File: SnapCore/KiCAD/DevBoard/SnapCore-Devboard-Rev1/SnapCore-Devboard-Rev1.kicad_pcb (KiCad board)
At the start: 4 copper layers, 26.8 x 55.9 mm, 58 parts, among them J2 USB_C_Receptacle_USB2.0_16P, J3 Conn_01x18_Pin, Q1 AO3407A, SW2 TS-1187A, U1 nRF52840-QIXX, U2 XC6220B331MR, U5 TP4056-42-ESOP8, Y1 32.768KHz, Y2 32MHz

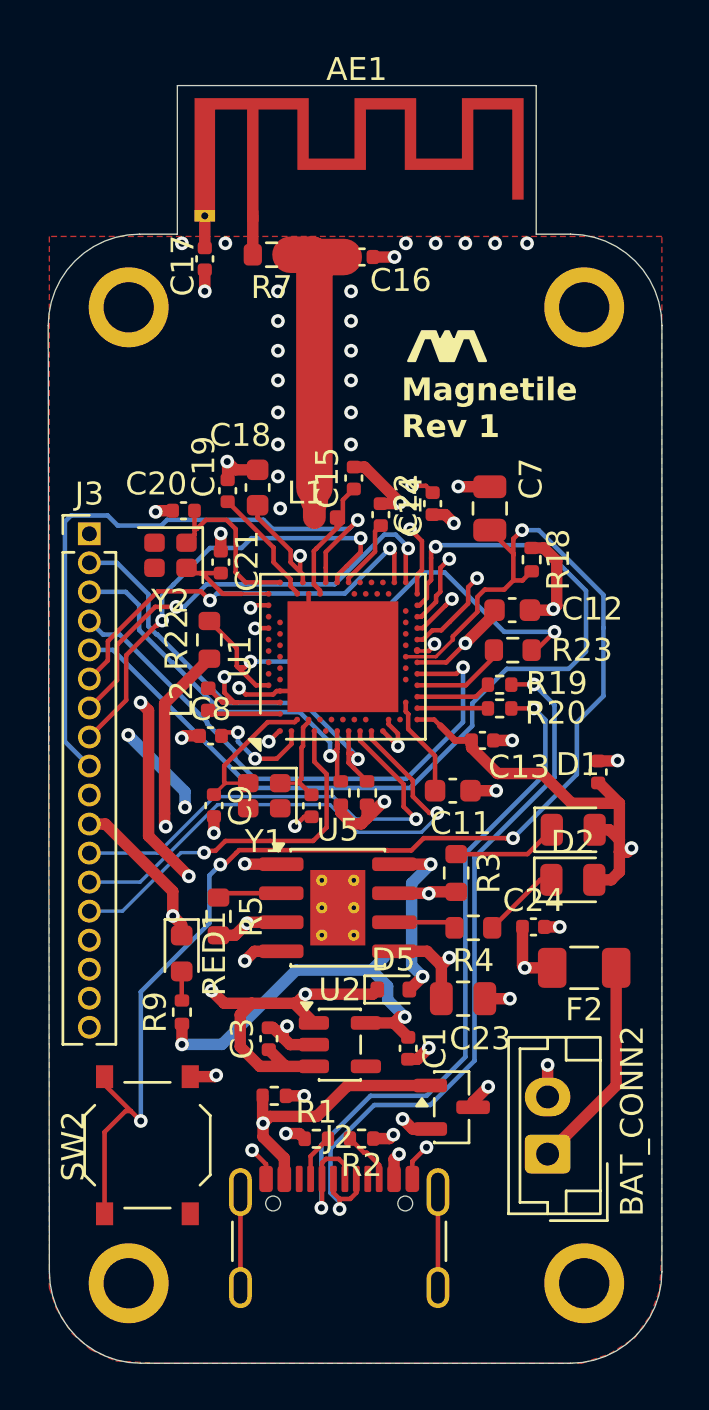
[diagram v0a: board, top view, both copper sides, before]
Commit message: Updated Devboard to use Chip Antenna instead of PCB Antenna for easier RF matching
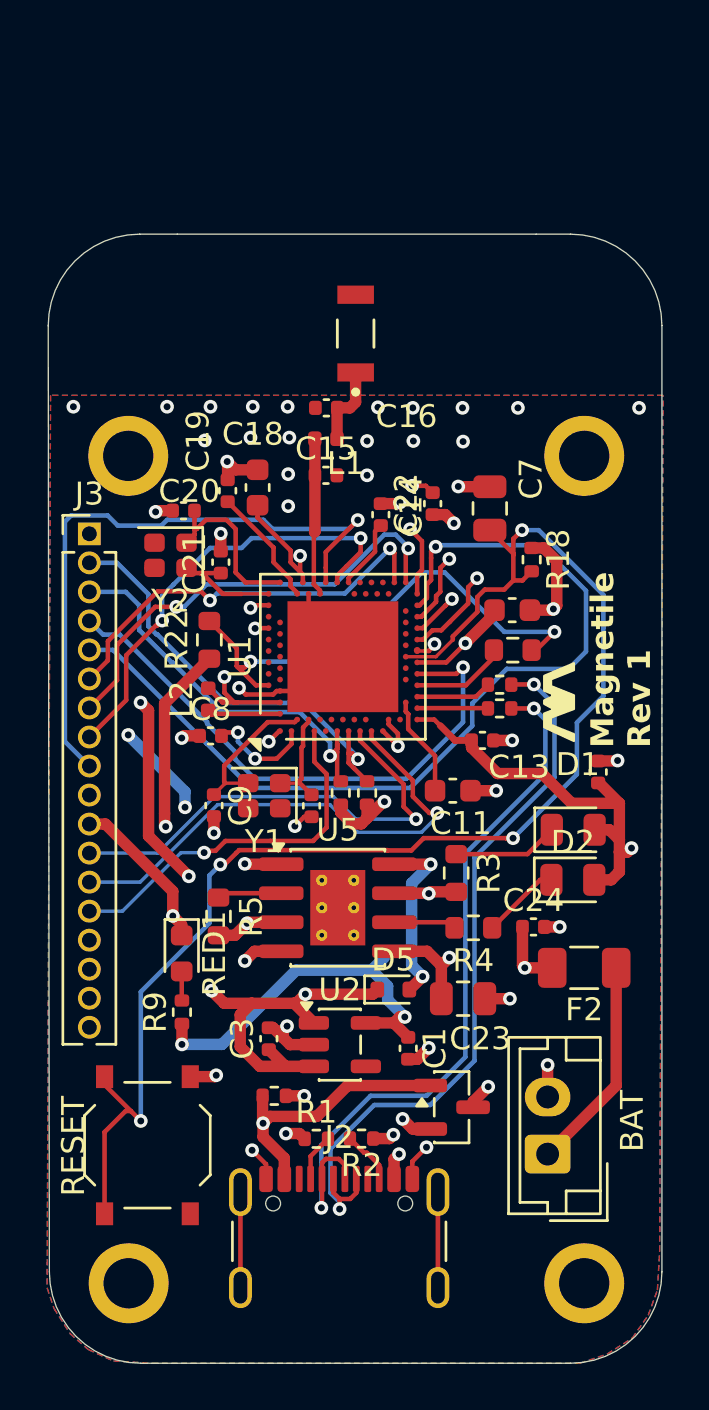
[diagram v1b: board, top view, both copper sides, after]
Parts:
- removed AE1: SWRA117D_2.4Ghz, RF_Antenna:Texas_SWRA117D_2.4GHz_Right
- removed C17: 1nF, Capacitor_SMD:C_0402_1005Metric
- removed R7: 0R, Resistor_SMD:R_0603_1608Metric
- added AE2: AMCA31-2R450G-S1F-T3, AMCA31-2R450G-S1F-T3:XDCR_AMCA31-2R450G-S1F-T3, F.Cu at (111.7, 86.5)
- moved H3 42.7 mm to (121.7, 128.0)
- moved H2 36.2 mm to (121.7, 91.8)
- moved C16 6.78 mm to (110.4, 89.7), turned to 180 degrees
- moved H4 6.50 mm to (101.8, 91.8)
- moved L1 3.45 mm to (110.4, 91.0), turned to 0 degrees
- moved C15 1.23 mm to (110.4, 92.7), turned to 0 degrees
- turned C21 to -90 degrees
- renumbered BAT_CONN2 to BAT, SW2 to RESET
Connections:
- C21 pad 1: XC2 -> GND
- C21 pad 2: GND -> XC2
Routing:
- net Net-(AE2-A): track 13.8 -> 3.56 mm
- net GND: track 67.6 -> 63.1 mm, vias 53 -> 49
- net Net-(AE1-FEED): track 1.70 -> 0.00 mm
- net Net-(AE1-PCB_Trace): track 1.40 -> 0.00 mm
- net ANT_H23: track 5.90 -> 6.92 mm
- added copper zone on B.Cu, net GND
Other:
- board size 26.8 x 55.9 mm -> 26.8 x 49.4 mm

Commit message: Removed unecessary silkscreen, Fixed small layout issue
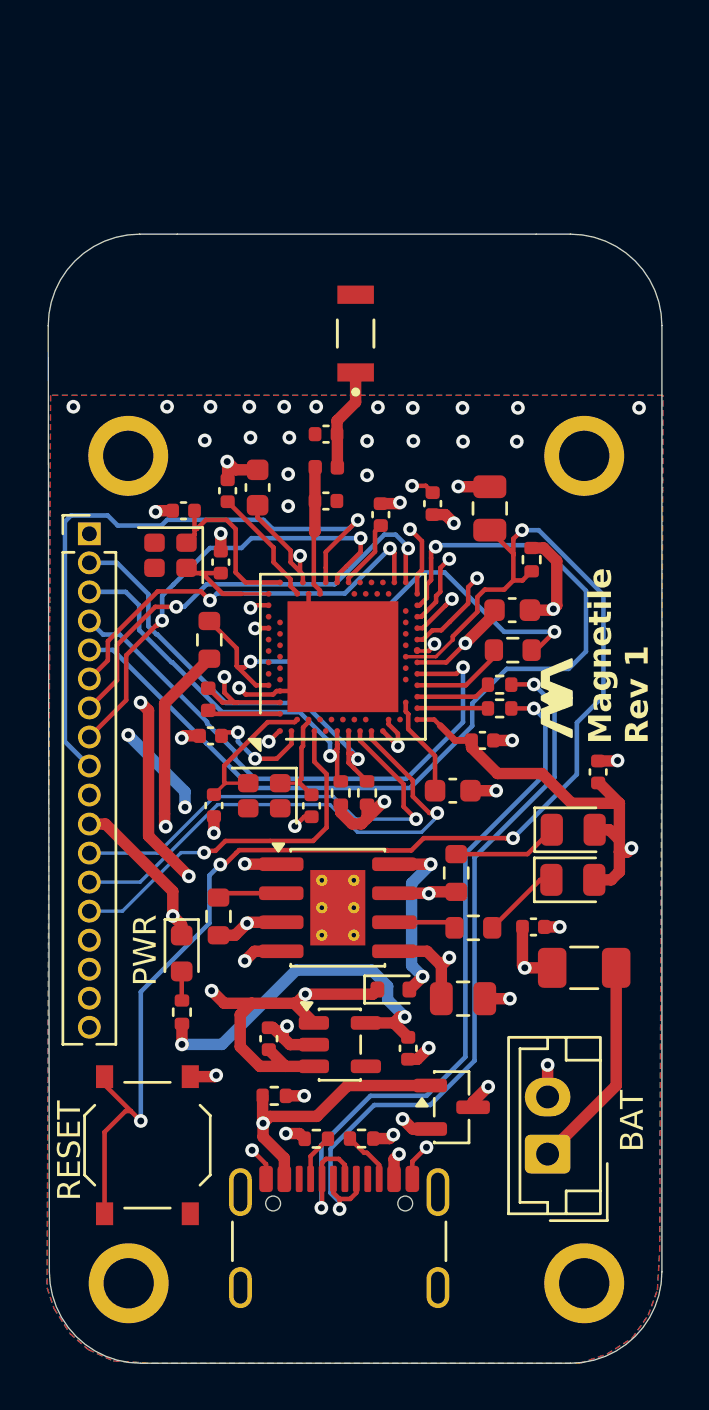
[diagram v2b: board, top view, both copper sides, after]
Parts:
- moved L1 1.25 mm to (110.4, 92.3)
- moved C16 1.15 mm to (110.4, 90.8)
- moved C15 1.12 mm to (110.4, 93.8)
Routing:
- net GND: track 63.1 -> 54.7 mm, vias 49 -> 51
- net ANT_H23: track 6.92 -> 5.70 mm
- net Net-(AE2-A): track 3.56 -> 4.49 mm
- net 3V3: track 99.5 -> 98.8 mm
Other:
- board text added: "PWR"

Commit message: Switched to TP4057 Charger IC, Added J4 to bottom pinout
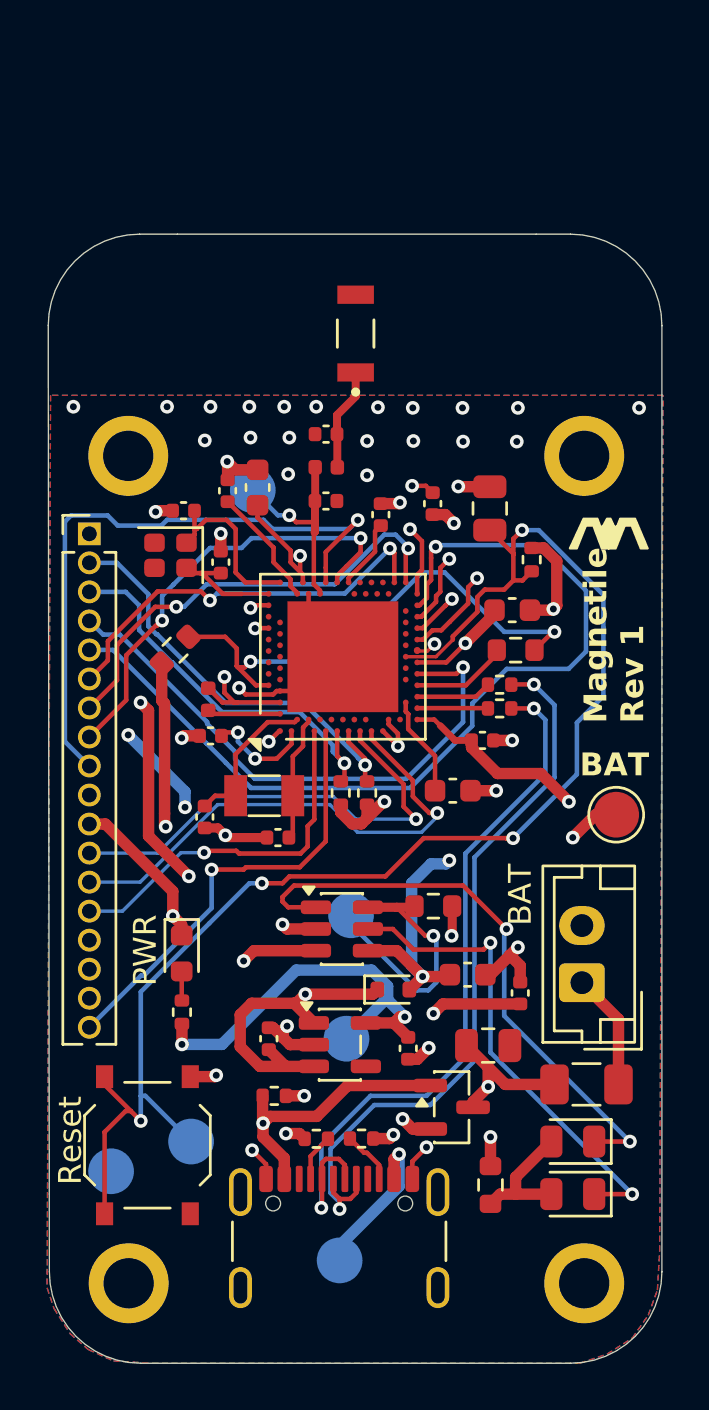
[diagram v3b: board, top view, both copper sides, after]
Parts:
- removed C2, C24: 10uF, Capacitor_SMD:C_0402_1005Metric
- removed C23: 2.2uF, Capacitor_SMD:C_0805_2012Metric
- removed D1: Red, LED_SMD:LED_0805_2012Metric
- removed D2: Green, LED_SMD:LED_0805_2012Metric
- removed F2: 500mA, Fuse:Fuse_1206_3216Metric
- removed R22: 1M_1%, Resistor_SMD:R_0603_1608Metric
- removed R23: 510k_1%, Resistor_SMD:R_0603_1608Metric
- removed R3, R4: 1k, Resistor_SMD:R_0603_1608Metric
- removed R5: 4k, Resistor_SMD:R_0603_1608Metric
- removed U5: TP4056-42-ESOP8, Package_SO:SOIC-8-1EP_3.9x4.9mm_P1.27mm_EP2.41x3.3mm_ThermalVias
- added C4: 2.2uF, Capacitor_SMD:C_0805_2012Metric, F.Cu at (117.5, 117.6)
- added C5: 10uF, Capacitor_SMD:C_0402_1005Metric, F.Cu at (118.9, 115.3)
- added C6: 2.2uF, Capacitor_SMD:C_0603_1608Metric, F.Cu at (116.6, 114.5)
- added D3: Green, LED_SMD:LED_0805_2012Metric, F.Cu at (121.2, 124.1)
- added D4: Red, LED_SMD:LED_0805_2012Metric, F.Cu at (121.2, 121.8)
- added F1: 500mA, Fuse:Fuse_1206_3216Metric, F.Cu at (121.8, 119.3)
- added G***: LOGO, Pictures:FixedLogoFlipped, F.Cu at (111.4, 100.7)
- added R10: 1M_1%, Resistor_SMD:R_0603_1608Metric, F.Cu at (103.8, 100.3)
- added R11: 510k_1%, Resistor_SMD:R_0603_1608Metric, F.Cu at (118.7, 100.3)
- added R7: 330R, Resistor_SMD:R_0603_1608Metric, F.Cu at (117.6, 123.7)
- added R8: 4k, Resistor_SMD:R_0603_1608Metric, F.Cu at (115.1, 111.5)
- added TP1: VBUS, TestPoint:TestPoint_Pad_D2.0mm, B.Cu at (111.0, 127.0)
- added TP2: VBAT, TestPoint:TestPoint_Pad_D2.0mm, F.Cu at (123.1, 107.5)
- added TP3: 3V3, TestPoint:TestPoint_Pad_D2.0mm, B.Cu at (111.3, 117.3)
- added TP4: GND, TestPoint:TestPoint_Pad_D2.0mm, B.Cu at (101.0, 123.1)
- added TP5: RESET, TestPoint:TestPoint_Pad_D2.0mm, B.Cu at (104.5, 121.8)
- added TP6: RF, TestPoint:TestPoint_Pad_D2.0mm, B.Cu at (107.2, 93.3)
- added TP7: PROG, TestPoint:TestPoint_Pad_D2.0mm, B.Cu at (111.5, 111.9)
- added U4: TP4057, Package_TO_SOT_SMD:TSOT-23-6, F.Cu at (111.1, 112.5)
- C7: value 100NF -> 100nF
- Y1: footprint Crystal:Crystal_SMD_2016-4Pin_2.0x1.6mm -> Crystal:Crystal_SMD_3215-2Pin_3.2x1.5mm
- moved BAT 7.65 mm to (121.6, 114.8)
- moved C10 2.02 mm to (108.3, 108.5), turned to 180 degrees
- moved C9 0.64 mm to (105.1, 107.6)
- turned Y1 to 0 degrees
- renumbered RESET to SW2
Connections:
- J3 pad 18: GND -> P0.04_AIN2_A4_D4
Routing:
- net Net-(D4-K): track 0.00 -> 25.7 mm, vias 0 -> 2
- net Net-(D3-K): track 0.00 -> 21.1 mm, vias 0 -> 2
- net P0.04_AIN2_A4_D4: track 0.00 -> 19.5 mm, vias 0 -> 1
- net BAT0: track 43.4 -> 57.4 mm, vias 4 -> 5
- net Net-(U4-PROG): track 0.00 -> 11.7 mm, vias 0 -> 1
- net VBUS: track 101.6 -> 108.6 mm
- net Net-(D3-A): track 0.00 -> 5.79 mm
- net Net-(D1-K): track 4.66 -> 0.00 mm
- net Net-(BAT_CONN1-Pin_1): track 9.39 -> 5.11 mm
- net GND: track 54.7 -> 50.8 mm, vias 51 -> 45
- net Net-(D2-K): track 3.46 -> 0.00 mm
- net ANT_H23: track 5.70 -> 9.02 mm, vias 0 -> 1
- net Net-(U5-PROG): track 2.82 -> 0.00 mm
- net Net-(U5-~{STDBY}): track 2.73 -> 0.00 mm
- net 3V3: track 98.8 -> 101.2 mm
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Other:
- board text added: "3V3"
- board text added: "BAT"
- board text added: "GND"
- board text added: "PROG"
- board text added: "RESET"
- board text added: "RF"
- board text added: "Reset"
- board text added: "VBUS"
